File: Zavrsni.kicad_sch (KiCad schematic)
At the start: 37 parts, among them K1 JST-2pin-SMD, SW1 SW_Push, SW2 SW_Push

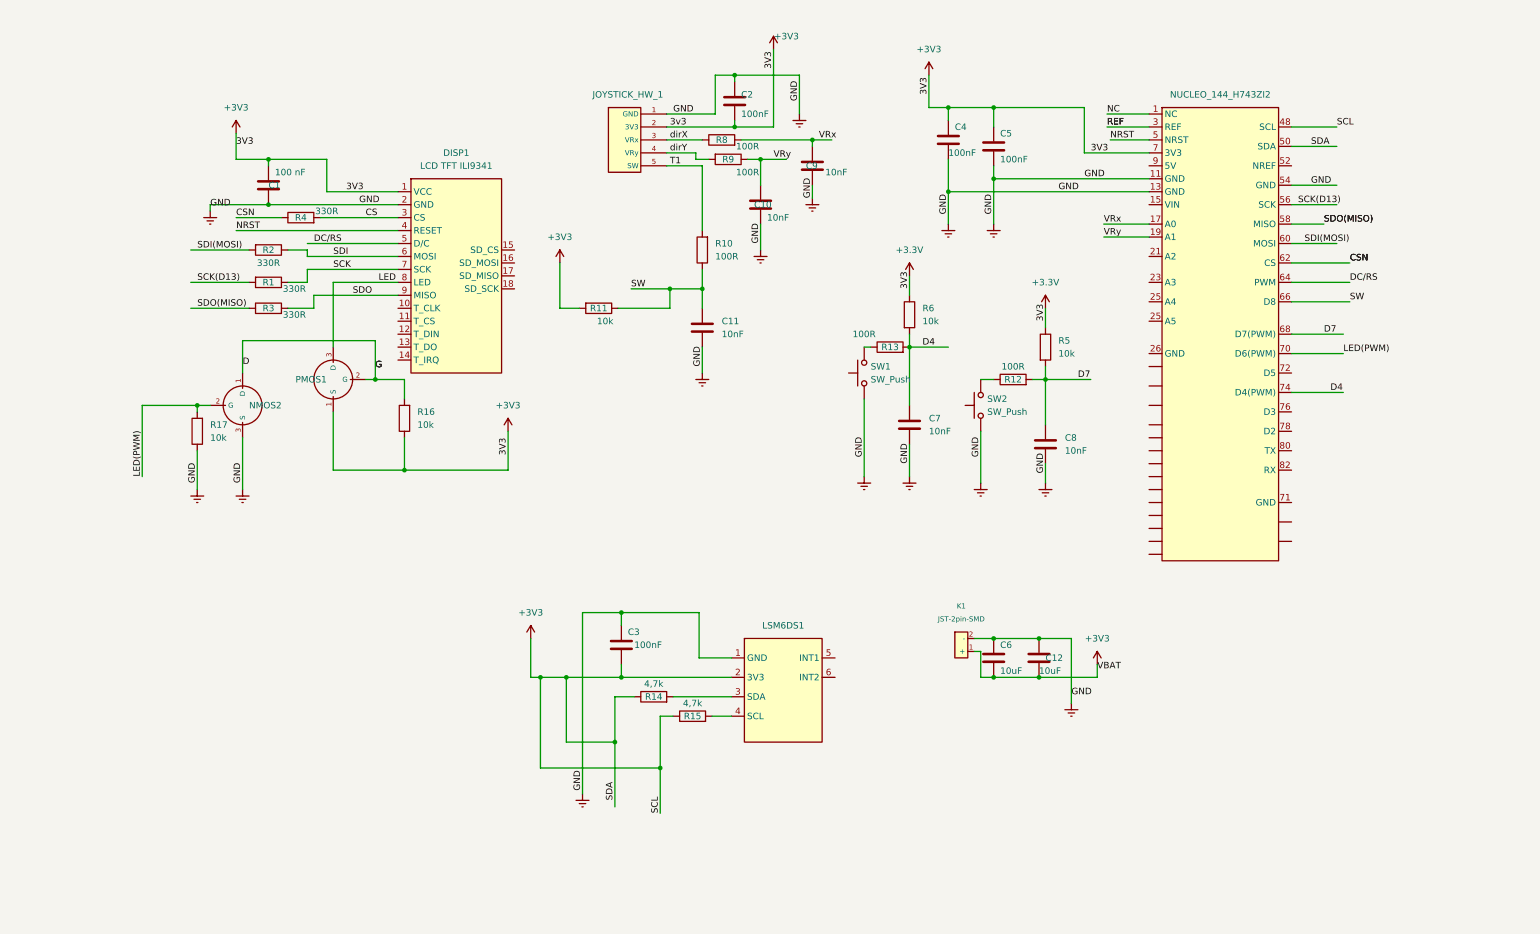
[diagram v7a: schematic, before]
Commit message: [ladyM9]  LSM is placed on the bottom side of the PCB, vias are reduced, buttons are placed and connected to the PCB
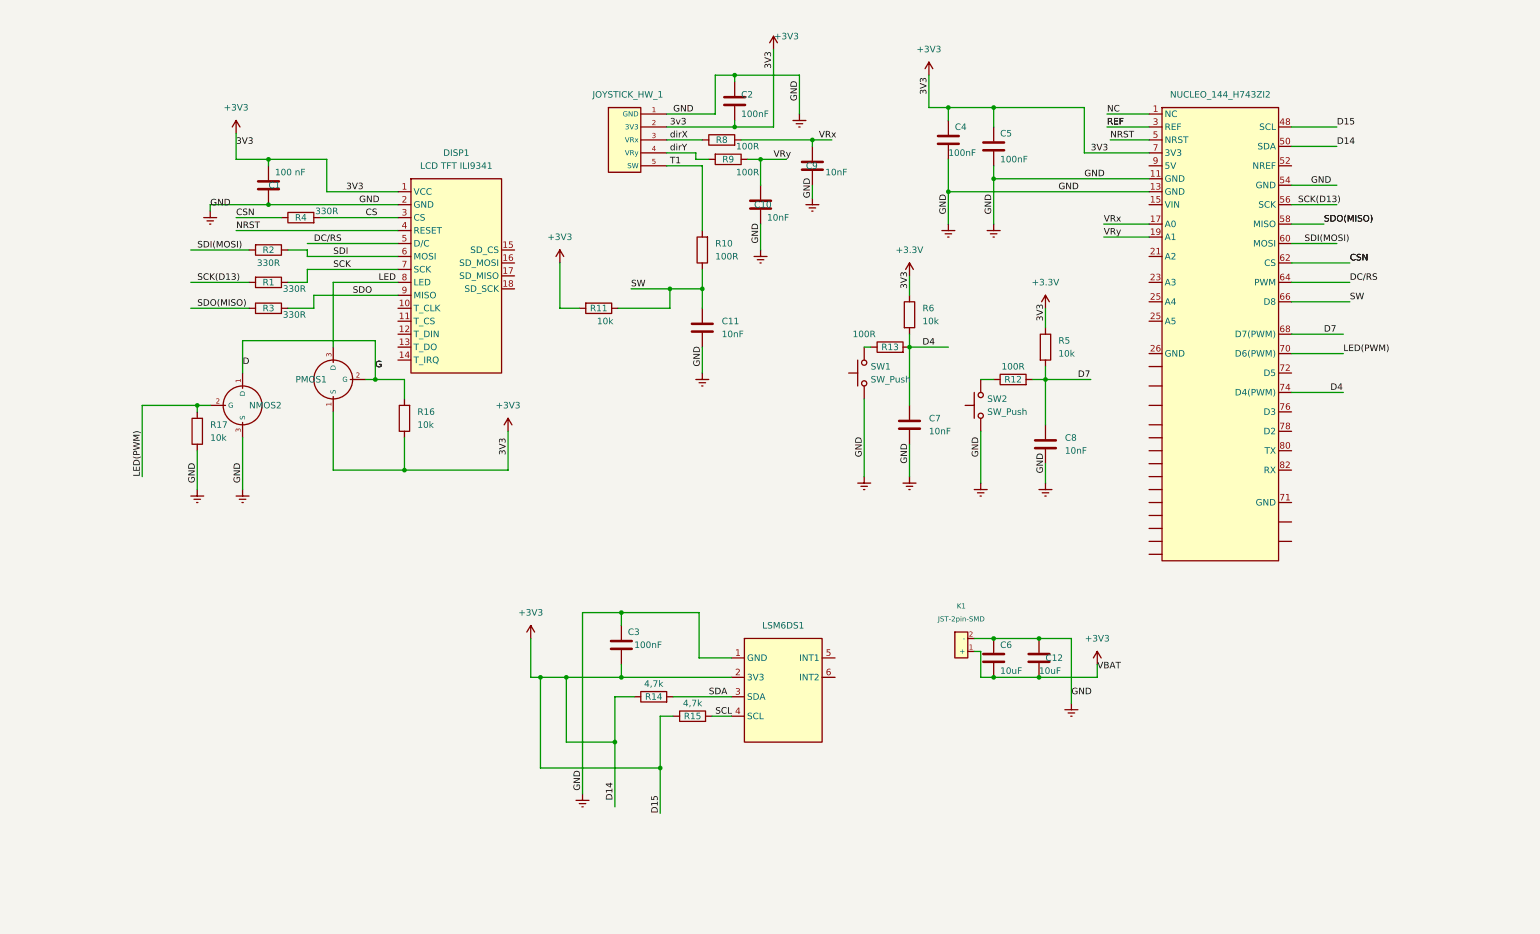
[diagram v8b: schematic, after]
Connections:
- net SCL: now reaches LSM6DS1.4 (SCL), R15.2
- net SDA: now reaches LSM6DS1.3 (SDA), R14.2
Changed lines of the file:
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@@
     (effects (font (size 1.27 1.27)) (justify left bottom))
   )
-  (label "SDA" (at 130.175 171.45 90) (fields_autoplaced)
+  (label "D14" (at 130.175 171.45 90) (fields_autoplaced)
     (effects (font (size 1.27 1.27)) (justify left bottom))
   )
@@
     (effects (font (size 1.27 1.27)) (justify left bottom))
   )
-  (label "SCL" (at 139.065 173.99 90) (fields_autoplaced)
+  (label "D15" (at 139.065 173.99 90) (fields_autoplaced)
     (effects (font (size 1.27 1.27)) (justify left bottom))
   )
   (label "GND" (at 57.15 109.22 90) (fields_autoplaced)
+    (effects (font (size 1.27 1.27)) (justify left bottom))
+  )
+  (label "SCL" (at 149.86 154.94 0) (fields_autoplaced)
     (effects (font (size 1.27 1.27)) (justify left bottom))
   )
@@
   )
   (label "VRx" (at 226.06 58.42 0) (fields_autoplaced)
-    (effects (font (size 1.27 1.27)) (justify left bottom))
-  )
-  (label "SCL" (at 271.78 39.37 0) (fields_autoplaced)
     (effects (font (size 1.27 1.27)) (justify left bottom))
   )
@@
     (effects (font (size 1.27 1.27)) (justify left bottom))
   )
+  (label "D15" (at 271.78 39.37 0) (fields_autoplaced)
+    (effects (font (size 1.27 1.27)) (justify left bottom))
+  )
   (label "SCK" (at 74.93 67.31 0) (fields_autoplaced)
     (effects (font (size 1.27 1.27)) (justify left bottom))
@@
   )
   (label "SDO(MISO)" (at 48.26 74.93 0) (fields_autoplaced)
+    (effects (font (size 1.27 1.27)) (justify left bottom))
+  )
+  (label "SDA" (at 148.59 151.13 0) (fields_autoplaced)
     (effects (font (size 1.27 1.27)) (justify left bottom))
   )
@@
     (effects (font (size 1.27 1.27)) (justify left bottom))
   )
-  (label "SDA" (at 266.7 43.18 0) (fields_autoplaced)
-    (effects (font (size 1.27 1.27)) (justify left bottom))
-  )
   (label "3V3" (at 109.22 100.33 270) (fields_autoplaced)
     (effects (font (size 1.27 1.27)) (justify right bottom))
@@
     (effects (font (size 1.27 1.27)) (justify left bottom))
   )
+  (label "D14" (at 271.78 43.18 0) (fields_autoplaced)
+    (effects (font (size 1.27 1.27)) (justify left bottom))
+  )
